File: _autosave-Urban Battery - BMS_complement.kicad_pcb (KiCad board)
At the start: 2 copper layers, 154 x 84.1 mm, 58 parts, among them J1 BMS IO, J10 E-Stop, J11 Contactor Connector, J12 Thermistor, J13 Thermistor, J14 Thermistor, J15 short pins, J16 short pins, J17 short pins, J18 short pins, J19 Test-pins, J2 OLED Header, J20 Test-pins, J21 Test-pins, J22 Test-pins, J23 Test-pins, J24 Test-pins, J25 Test-pins, J26 Test-pins, J27 Test-pins, J28 Test-pins, J3 CAN, J4 CAN, J5 Charge Connector, J6 Battery Connector, J7 E-Stop, J8 E-Stop, J9 E-Stop, K1 Charge_Relay, K2 Contactor_Relay, SW1 SW_SPST, SW2 SW_DPDT_x2, SW3 CAN_TERM, U1 MCP2515-I/SO, U2 MCP2561/2, U3 LM2576HVS-12, Y1 8MHz

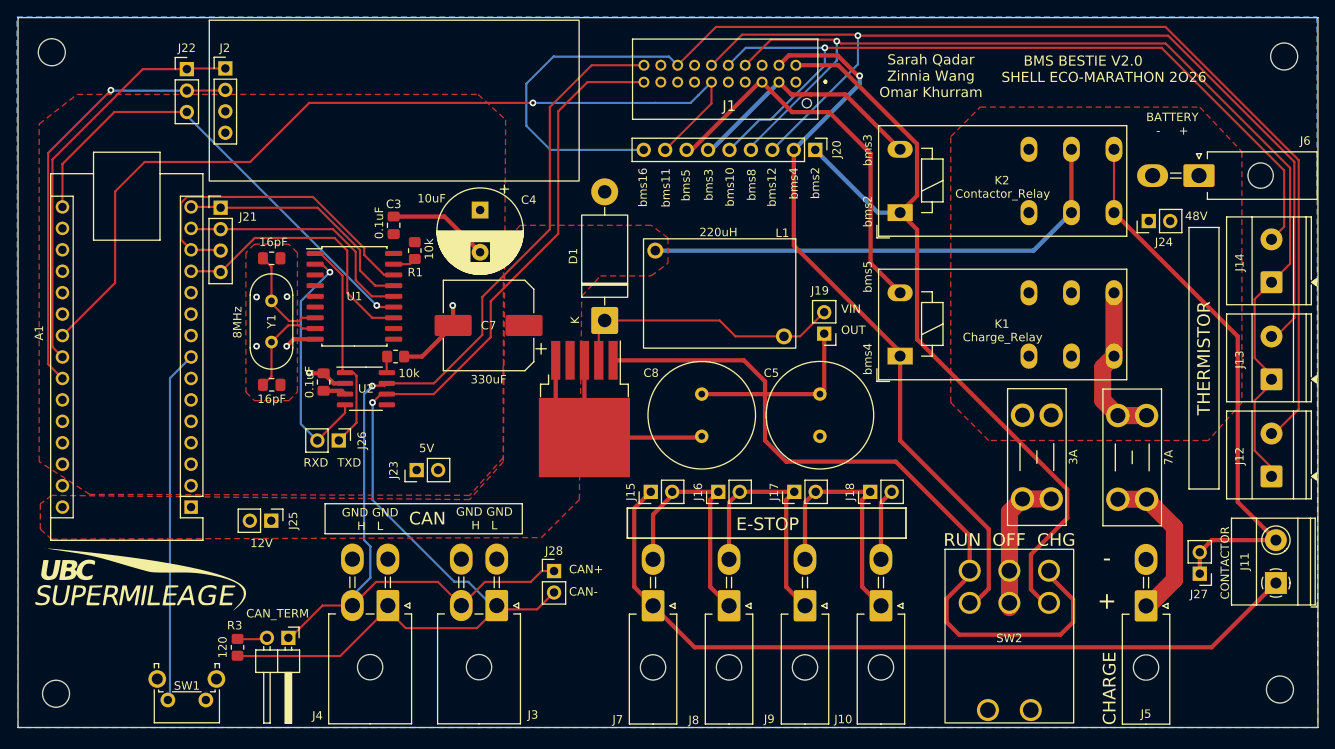
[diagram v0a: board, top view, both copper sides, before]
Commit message: added chamfered edges on fill zones. fixed issue of GND fill zone on crystal, and also fixed GND pin on BMS I/O being cut-off from the GND plane
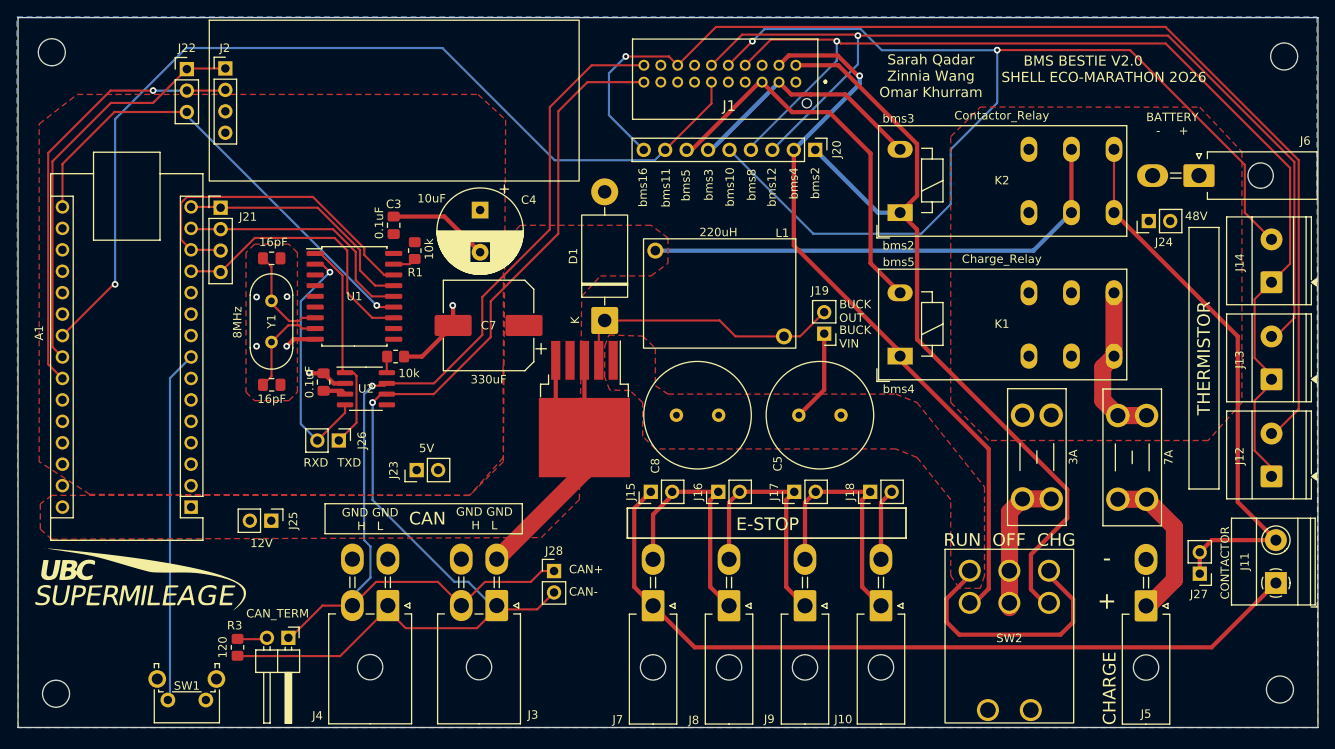
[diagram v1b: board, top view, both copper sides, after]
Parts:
- moved C8 3.91 mm to (152.5, 99.5), turned to 0 degrees
- moved C5 3.54 mm to (167.0, 99.5), turned to 0 degrees
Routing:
- net Buck_VIN: track 110.6 -> 40.5 mm
- net bms10: track 98.5 -> 132.2 mm, vias 1 -> 2
- net bms16: track 155.3 -> 135.8 mm, vias 0 -> 1
- net bms11: track 106.0 -> 113.3 mm
- added copper zone on F.Cu, net Buck_VIN
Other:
- board text added: "BUCK OUT"
- board text added: "BUCK VIN"
- board text removed: "OUT"
- board text removed: "VIN"
